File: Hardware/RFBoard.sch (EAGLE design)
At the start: 388 parts, among them IC1 HMC1097, IC10 NCP702-1.8, IC11 TPS42951, IC12 MCP4812, IC13 STM32F030C8T, IC14 LT5560, IC15 ADF4360, IC16 HMC284, IC17 HMC284, IC18 NCP702-3.3, IC19 NCP702-3.3, IC2 MAX2871, IC20 LT1395, IC21 MAADSS0008, IC22 MAADSS0008, IC23 MAADSS0008, IC24 RFSA2033, IC25 MMG3H21NT1, IC26 MMG3H21NT1, IC27 HMC1021, IC28 MCP4812, IC29 NCP702-3.3, IC3 AP2114HA-3.3, IC31 QPC6064, IC32 QPC6064, IC4 NCP702-3.3, IC5 NCP702-3.3, IC6 MAX5873, IC7 NCP702-1.8, IC8 NCP702-3.3, IC9 NCP702-3.3, Q1 BSS123, Q2 BSS123, Q3 BSS123, Q4 BSS123, Q5 BSS123, Q6 BSS84, U1 6SLX9TQG144, U4 W25Q16BVSN, X1 out, X2 FH12-20S-0.5SH

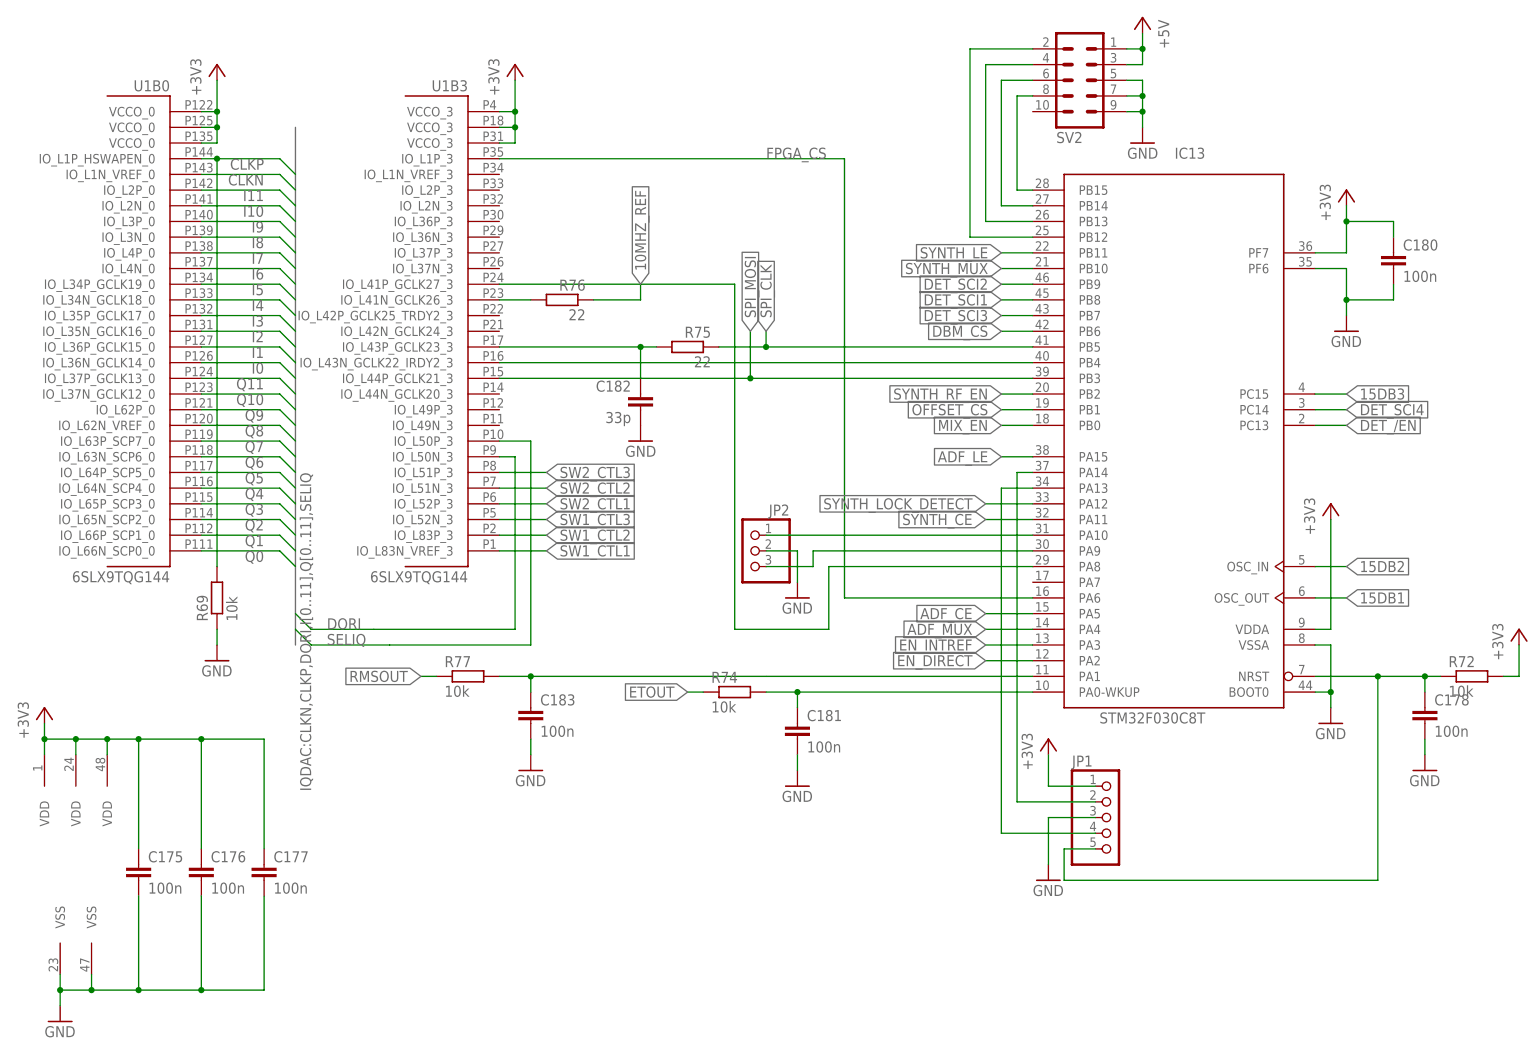
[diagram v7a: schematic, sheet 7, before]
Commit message: Silkscreen, MOD_EN wire
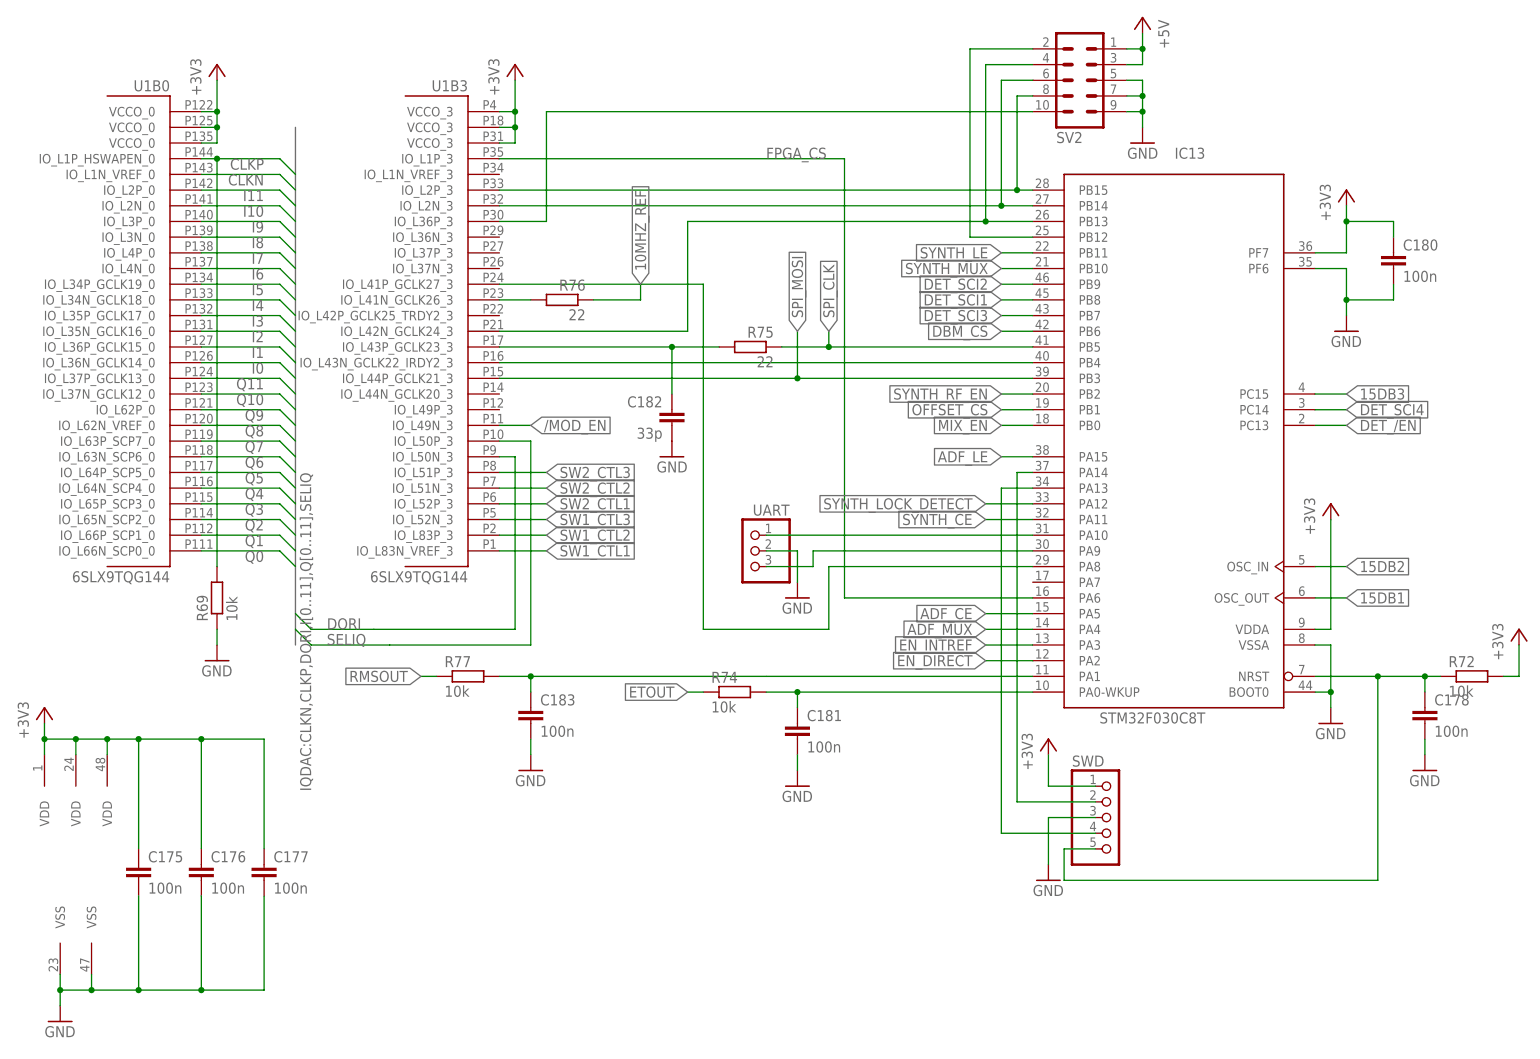
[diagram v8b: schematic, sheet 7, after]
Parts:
- renumbered JP1 to SWD, JP2 to UART, SV1 to JTAG, U$1 to B1
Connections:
- net N$178 renamed RX
- net N$179 renamed TX
- net N$180 renamed SWCLK
- net N$182 renamed SWDIO
- net N$183 renamed NRST
- net N$185 renamed CS
- removed net N$186: IC13MCU.PB15, SV2.8
- removed net N$187: IC13MCU.PB14, SV2.6
- removed net N$188: IC13MCU.PB13, SV2.4
- new net CS_FPGA: SV2.10, U1B3.IO_L36P_3
- new net MISO: IC13MCU.PB14, SV2.6, U1B3.IO_L2N_3
- new net MOSI: IC13MCU.PB15, SV2.8, U1B3.IO_L2P_3
- new net SCK: IC13MCU.PB13, SV2.4, U1B3.IO_L42N_GCLK24_3
- net /MOD_EN: now also U1B3.IO_L49N_3
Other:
- moved on the sheet: C182, R75
